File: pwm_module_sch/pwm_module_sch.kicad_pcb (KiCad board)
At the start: 2 copper layers, 49 parts, among them J1 SWIMM, J2 output -, J3 input, J4 output+, J5 uart, Q1 AO3400, Q2 6N60, SW1 ., SW2 ., U1 TM1637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

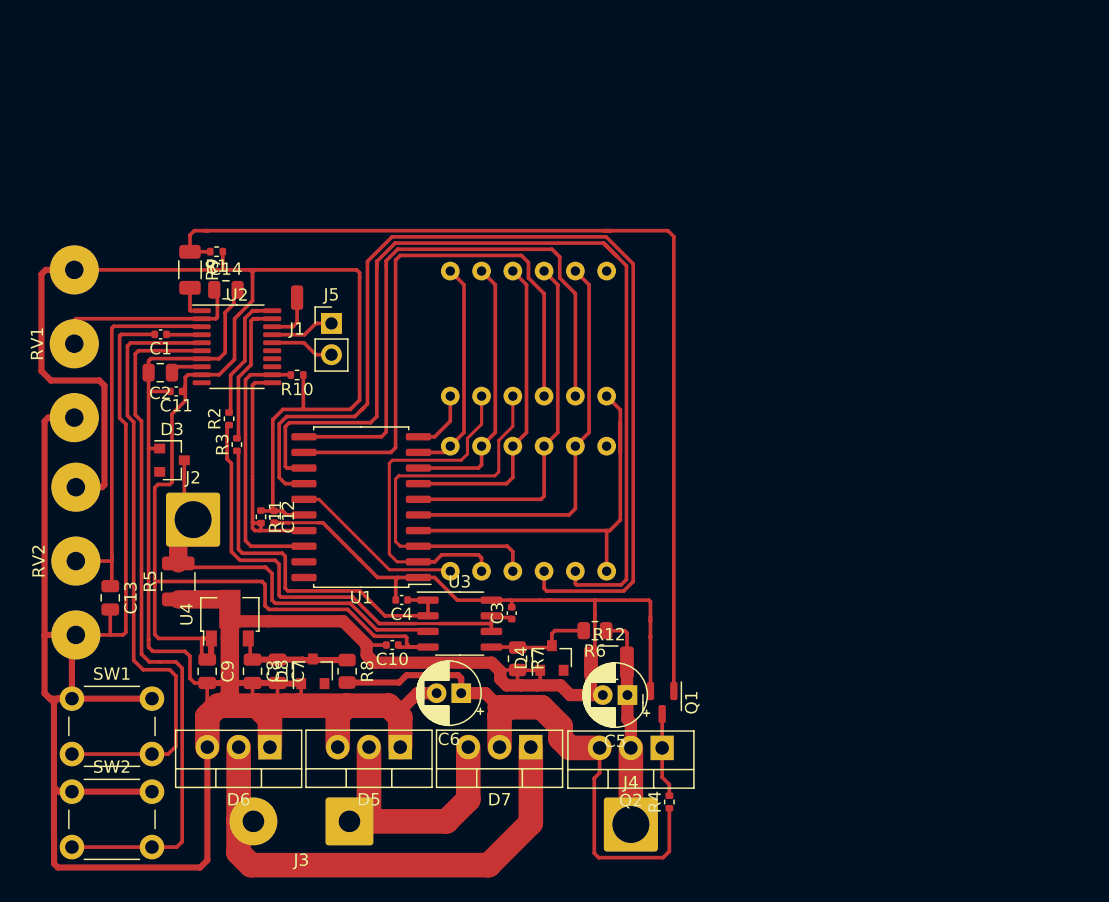
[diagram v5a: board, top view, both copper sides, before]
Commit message: 10A shunt
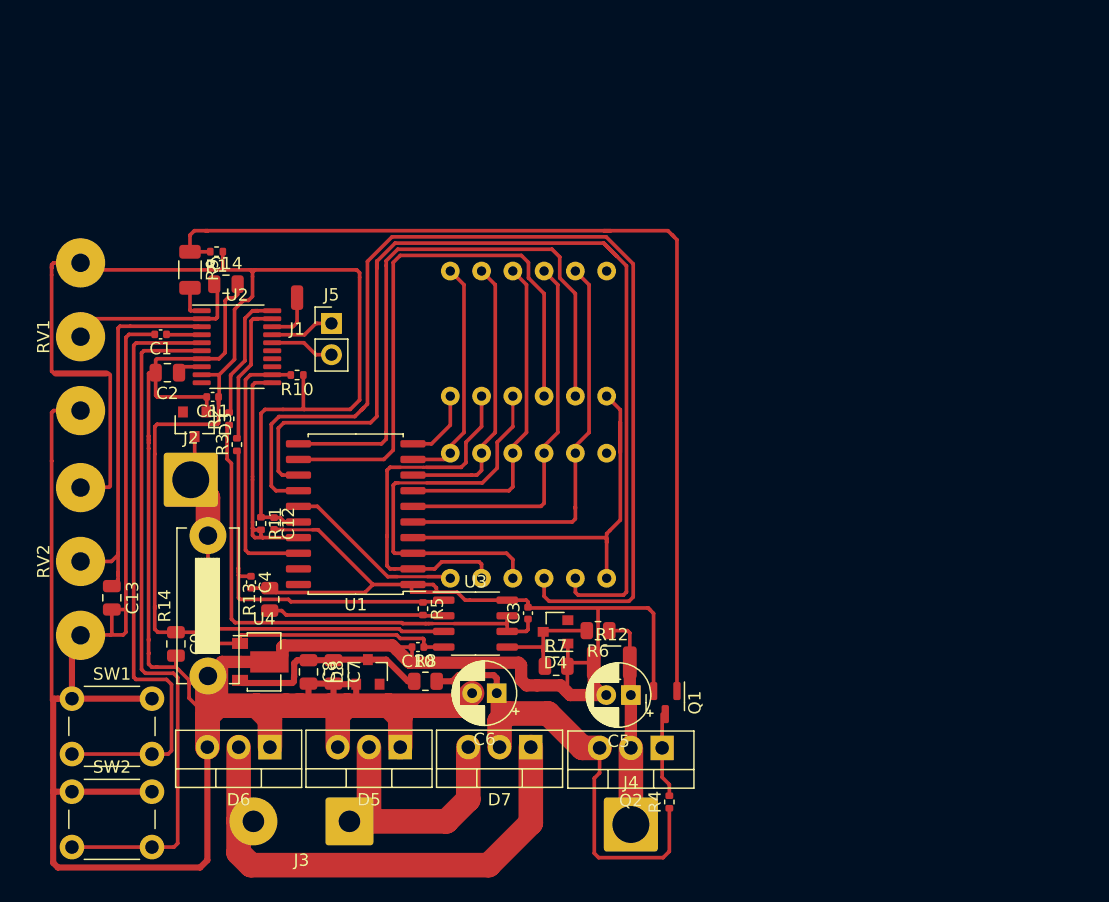
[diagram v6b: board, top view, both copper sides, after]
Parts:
- added R13: 5.1k, Resistor_SMD:R_0805_2012Metric, F.Cu at (201.7, 79.2)
- added R14: 0.01R, Resistor_THT:R_Bare_Metal_Element_L12.4mm_W4.8mm_P11.40mm, F.Cu at (196.7, 85.5)
- R5: value 0.1R -> 100k; footprint Resistor_SMD:R_1210_3225Metric -> Resistor_SMD:R_0402_1005Metric
- moved R5 20.0 mm to (214.1, 80.0), turned to 270 degrees
- moved C4 12.3 mm to (200.2, 77.9), turned to 270 degrees
- moved R8 6.41 mm to (214.3, 85.9), turned to 0 degrees
- moved C8 4.55 mm to (204.8, 85.1)
- moved C7 4.55 mm to (206.9, 85.1)
- moved D8 4.47 mm to (209.7, 85.1)
- moved U4 4.33 mm to (200.9, 84.3), turned to 0 degrees
- moved D3 3.45 mm to (195.6, 65.0), turned to 270 degrees
- moved C9 3.38 mm to (194.1, 82.9)
- moved J2 3.24 mm to (195.3, 69.5)
- moved R7 3.20 mm to (224.9, 84.7), turned to 0 degrees
- moved C11 2.99 mm to (197.0, 62.8)
- moved C6 2.88 mm to (220.1, 86.9)
- moved D4 2.14 mm to (224.9, 81.9), turned to 180 degrees
- moved C10 2.09 mm to (213.7, 83.1)
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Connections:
- R5 pad 1: GND -> Net-(C4-Pad1)
- R5 pad 2: -VSW -> Net-(R13-Pad1)
- U3 pad 2: Net-(C4-Pad1) -> Net-(R13-Pad1)
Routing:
- net GND: track 328.7 -> 345.8 mm
- net Net-(R13-Pad1): track 0.00 -> 14.3 mm
- net +24V: track 49.4 -> 39.3 mm
- net +3V3: track 158.1 -> 150.5 mm
- net Net-(C7-Pad1): track 9.86 -> 16.9 mm
- net Net-(C3-Pad1): track 39.0 -> 42.5 mm
- net Net-(D2-Pad9): track 84.4 -> 86.9 mm
- net -VSW: track 33.0 -> 35.4 mm
- net Net-(D2-Pad8): track 79.7 -> 81.7 mm
- net Net-(D1-Pad5): track 33.2 -> 34.5 mm
- net Net-(D1-Pad1): track 18.1 -> 19.3 mm
- net Net-(SW2-Pad2): track 57.1 -> 56.1 mm
- net Net-(D1-Pad8): track 48.2 -> 49.2 mm
- net Net-(D1-Pad11): track 30.6 -> 29.6 mm
- net Net-(D1-Pad12): track 5.15 -> 6.01 mm
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
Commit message: board ok
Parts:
- Q2: value 6N60 -> IRFZ44N
- R12: footprint Resistor_SMD:R_1210_3225Metric -> Resistor_SMD:R_1206_3216Metric
- moved R13 14.0 mm to (215.6, 80.3), turned to 0 degrees
- moved C4 12.9 mm to (213.0, 79.5), turned to 180 degrees
- moved Q1 8.57 mm to (233.6, 79.1), turned to 0 degrees
- moved R12 5.25 mm to (234.1, 86.9), turned to 270 degrees
- moved R6 3.94 mm to (232.3, 81.9)
- moved R5 3.75 mm to (217.9, 79.9)
- moved U3 3.73 mm to (222.1, 81.2)
- moved C3 3.72 mm to (226.4, 80.5)
- moved C10 3.71 mm to (217.4, 83.2)
- moved D4 3.71 mm to (228.6, 81.9)
- moved R7 3.66 mm to (228.6, 84.6)
- moved C7 1.42 mm to (208.3, 85.2)
- moved D8 1.42 mm to (211.1, 85.1)
- moved C5 1.33 mm to (232.0, 87.9), turned to 90 degrees
- moved C8 1.01 mm to (205.5, 85.9), turned to 0 degrees
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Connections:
- R13 pad 1: Net-(R13-Pad1) -> GND
- R13 pad 2: GND -> Net-(R13-Pad2)
- R5 pad 2: Net-(R13-Pad1) -> Net-(R13-Pad2)
- U3 pad 2: Net-(R13-Pad1) -> Net-(R13-Pad2)
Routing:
- net Net-(R13-Pad1): track 14.3 -> 0.00 mm
- net GND: track 345.8 -> 332.0 mm
- net Net-(Q1-Pad3): track 6.87 -> 19.8 mm
- net Net-(Q1-Pad1): track 80.9 -> 70.0 mm
- net Net-(C4-Pad1): track 30.4 -> 38.1 mm
- net +3V3: track 150.5 -> 155.9 mm
- net +VSW: track 17.2 -> 21.3 mm
- net -VSW: track 35.4 -> 39.5 mm
- net Net-(C3-Pad1): track 42.5 -> 46.6 mm
- net Net-(R13-Pad2): track 0.00 -> 3.82 mm
- net Net-(D4-Pad1): track 9.44 -> 10.8 mm
- net +24V: track 39.3 -> 38.4 mm

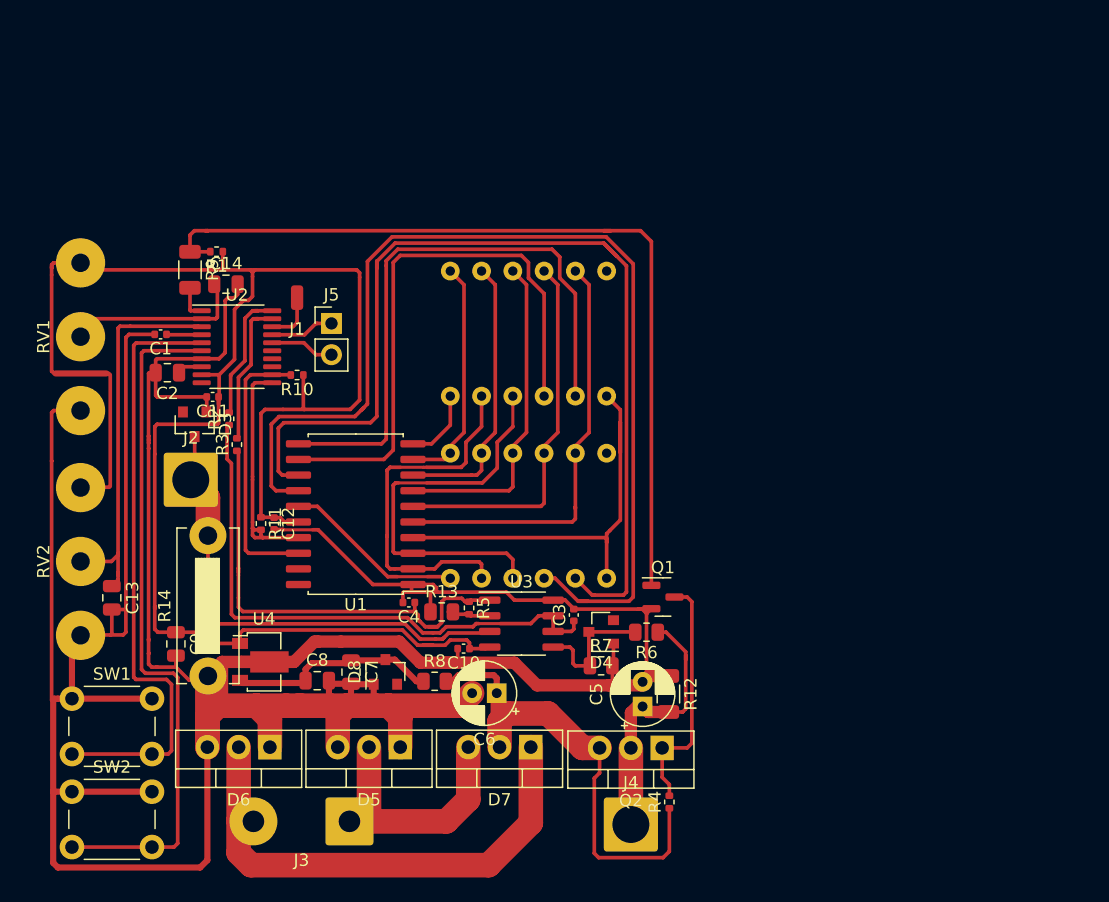
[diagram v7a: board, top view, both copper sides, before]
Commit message: working UART on board
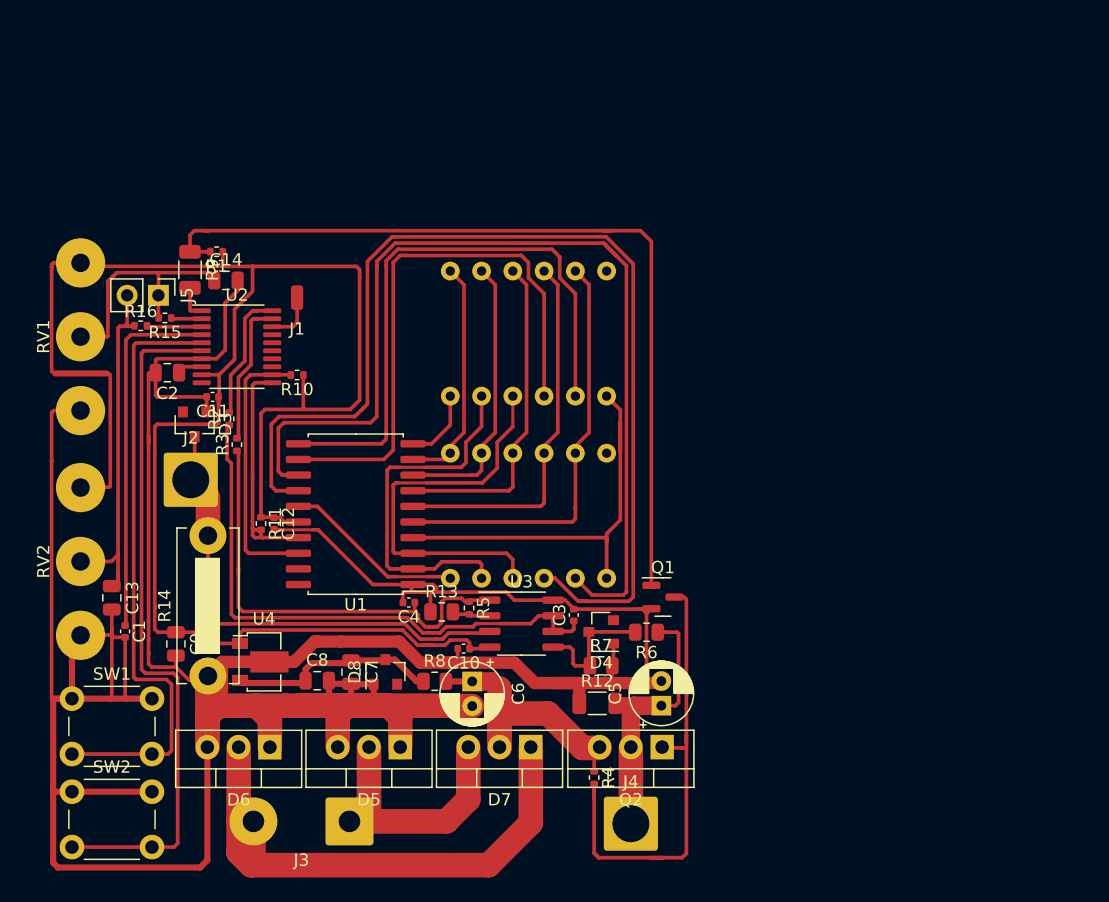
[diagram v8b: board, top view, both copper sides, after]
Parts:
- added R15: 75, Resistor_SMD:R_0402_1005Metric, F.Cu at (193.2, 56.4)
- added R16: 75, Resistor_SMD:R_0402_1005Metric, F.Cu at (191.2, 57.0)
- moved C1 24.3 mm to (189.9, 81.9), turned to 270 degrees
- moved J5 14.2 mm to (192.6, 54.5), turned to 270 degrees
- moved R4 6.42 mm to (228.0, 93.7), turned to 270 degrees
- moved R12 5.83 mm to (228.3, 87.7), turned to 0 degrees
- moved C6 2.21 mm to (218.1, 85.9), turned to 270 degrees
- moved C5 1.53 mm to (233.5, 87.9)
- moved C14 0.30 mm to (198.1, 53.3)
- moved J4 0.06 mm to (231.0, 97.5)
- moved Q2 0.06 mm to (233.6, 91.2)
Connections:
- J5 pad 1: Net-(J5-Pad1) -> Net-(C14-Pad1)
- J5 pad 2: Net-(J5-Pad2) -> Net-(C13-Pad1)
- U2 pad 16: Net-(J5-Pad2) -> Net-(U2-Pad16)
- U2 pad 17: Net-(J5-Pad1) -> Net-(U2-Pad17)
- U2 pad 2: Net-(C14-Pad1) -> Net-(R15-Pad1)
- U2 pad 3: Net-(C13-Pad1) -> Net-(R16-Pad2)
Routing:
- net Net-(C1-Pad1): track 2.87 -> 29.6 mm
- net Net-(Q1-Pad3): track 19.8 -> 40.5 mm
- net +24V: track 38.4 -> 23.5 mm
- net GND: track 332.0 -> 324.2 mm
- net Net-(J5-Pad2): track 5.22 -> 0.00 mm
- net Net-(J5-Pad1): track 5.20 -> 0.00 mm
- net Net-(R16-Pad2): track 0.00 -> 4.60 mm
- net Net-(D6-Pad2): track 47.8 -> 51.4 mm
- net Net-(C13-Pad1): track 31.8 -> 28.9 mm
- net Net-(C14-Pad1): track 17.3 -> 20.2 mm
- net Net-(R15-Pad1): track 0.00 -> 2.50 mm
- net +VSW: track 21.3 -> 22.9 mm
- net +3V3: track 155.9 -> 155.2 mm
